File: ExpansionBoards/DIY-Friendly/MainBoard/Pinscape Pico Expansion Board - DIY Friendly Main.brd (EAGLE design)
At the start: 160 x 107 mm, 115 parts, among them IC1 UCC27524P, IC10 ULN2803A, IC11 SN74HC165N, IC12 SN74HC165N, IC13 SN74HC74NE4, IC14 PC827, IC15 S-80833CLY, IC16 SN74HC165N, IC18 SN74HC165N, IC2 UCC27524P, IC3 UCC27524P, IC4 UCC27524P, IC5 UCC27524P, IC6 UCC27524P, IC7 ULN2803A, IC8 ULN2803A, IC9 ULN2803A, J1 30316-6002HBROTATED, J10 215079-4, J11 640454-2, J13 640445-2, J14 SSQ-108-02-T-S-RA, J2 640445-6, J3 640445-5, J4 640445-9, J5 1-640456-0, J6 1-640456-0, J7 1-640456-0, J8 1-640456-0, J9 30308-6002HB, Q1 STP19NF20, Q10 STP19NF20, Q11 STP19NF20, Q12 STP19NF20, Q13 BC337-25, Q15 2N5195G, Q16 2N2222A, Q2 FDPF085N10A, Q3 STP19NF20, Q4 STP19NF20, Q5 STP19NF20, Q6 STP19NF20, Q7 STP19NF20, Q8 STP19NF20, Q9 STP19NF20

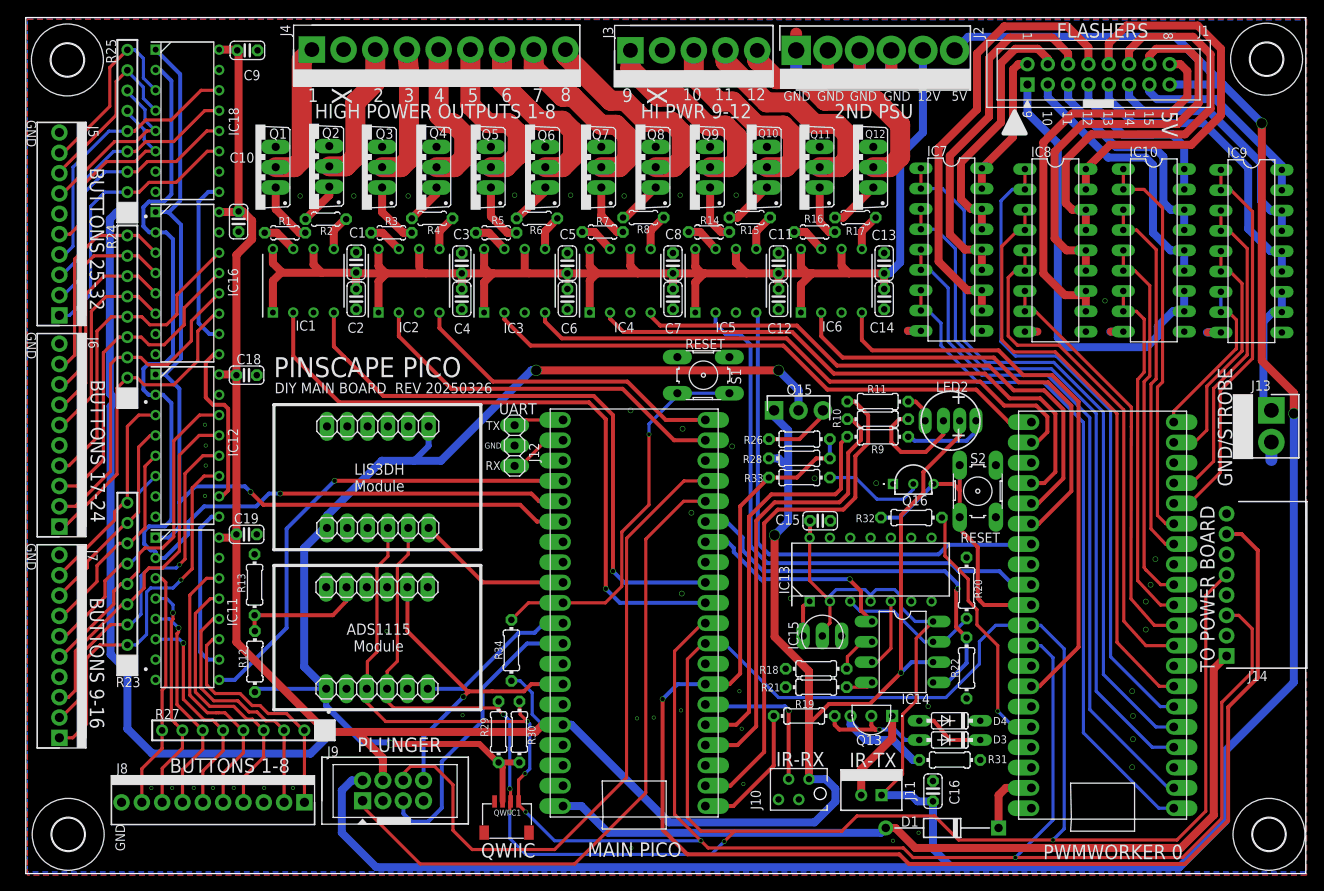
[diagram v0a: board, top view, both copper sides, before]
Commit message: Exp board: DIY main: improve reference designator ordering, fix bypass cap proximities to shift register chips, silkscreen cleanup
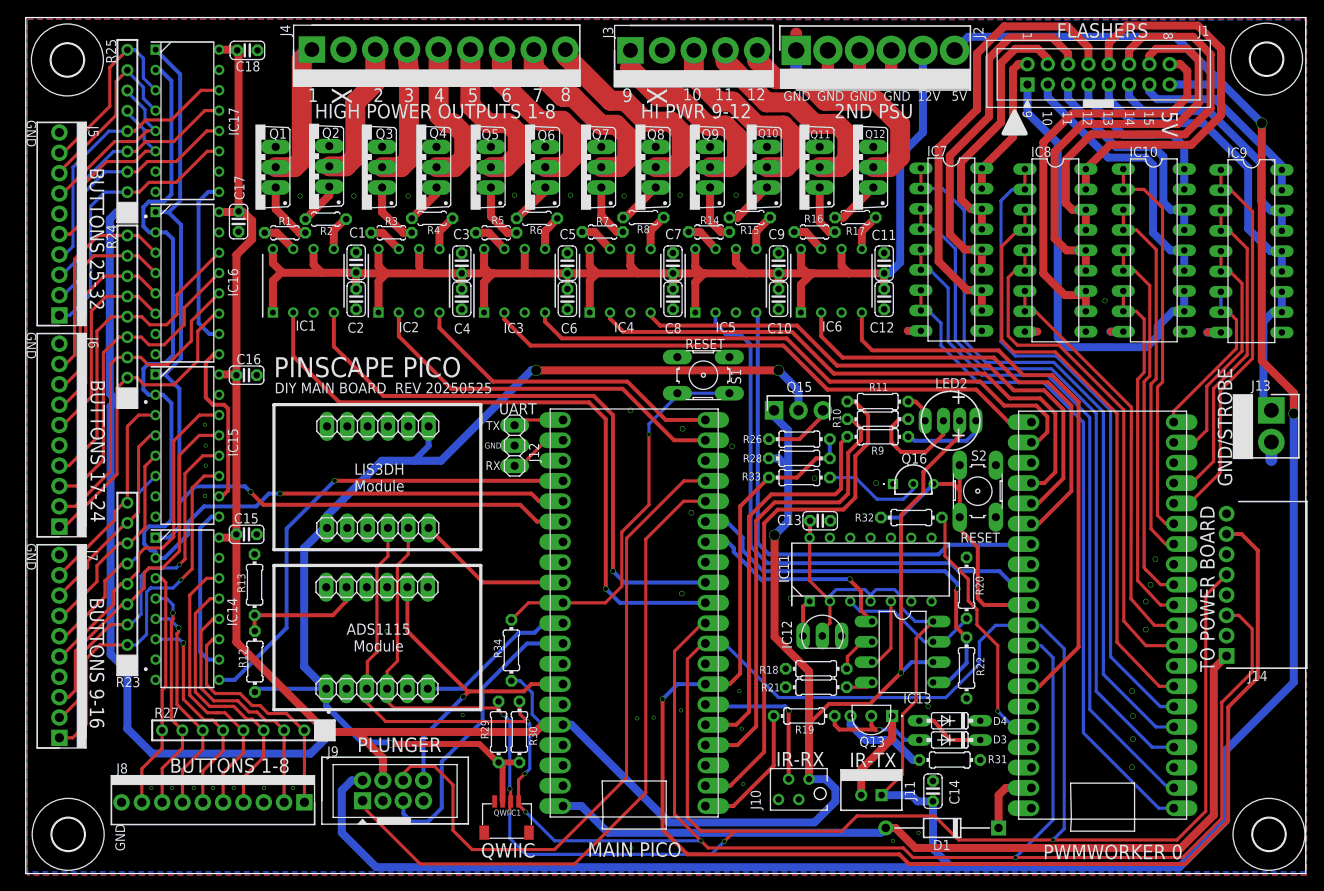
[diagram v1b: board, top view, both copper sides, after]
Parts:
- removed C19: 100nF, rcl:C025-024X044
- added C17: 100nF, rcl:C025-024X044
- C10, C7: value 100nF -> 4.7uF
- C16, C8: value 4.7uF -> 100nF
- IC11: value SN74HC165N -> SN74HC74NE4; device SamacSys_Parts:DIP794W53P254L1930H508Q16N -> SamacSys_Parts:DIP794W53P254L1930H508Q14N
- IC12: value SN74HC165N -> S-80833CLY; device SamacSys_Parts:DIP794W53P254L1930H508Q16N -> SamacSys_Parts:TO-92_(TO-226)
- IC13: value SN74HC74NE4 -> PC827; device SamacSys_Parts:DIP794W53P254L1930H508Q14N -> optocoupler:DIL08
- IC14: value PC827 -> SN74HC165N; device optocoupler:DIL08 -> SamacSys_Parts:DIP794W53P254L1930H508Q16N
- IC15: value S-80833CLY -> SN74HC165N; device SamacSys_Parts:TO-92_(TO-226) -> SamacSys_Parts:DIP794W53P254L1930H508Q16N
- moved C16 100.3 mm to (27.6, 57.3), turned to 180 degrees
- moved IC14 89.6 mm to (20.2, 28.1), turned to 0 degrees
- moved IC11 85.5 mm to (105.6, 33.0), turned to 90 degrees
- moved IC12 81.6 mm to (98.3, 24.7), turned to 180 degrees
- moved IC15 81.6 mm to (20.2, 48.5), turned to 0 degrees
- moved C15 71.7 mm to (27.6, 37.4), turned to 180 degrees
- moved C9 71.5 mm to (94.1, 71.3), turned to 270 degrees
- moved C10 68.2 mm to (94.1, 66.8)
- moved C14 61.8 mm to (113.4, 5.30)
- moved C18 40.6 mm to (27.7, 97.9)
- moved C13 33.2 mm to (99.3, 39.1), turned to 0 degrees
- moved C11 13.2 mm to (107.3, 71.3)
- moved C12 13.2 mm to (107.3, 66.8)
- moved IC13 11.0 mm to (109.6, 22.7), turned to 270 degrees
- moved C7 4.50 mm to (80.9, 71.3), turned to 270 degrees
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- renumbered IC18 to IC17
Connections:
- net 12V: now also C10.2, C9.2; no longer C13.2, C14.2
- net 3V3_PICO: now also C15.2, C16.2, C17.2, IC13.6, IC14.16, IC15.16; no longer C10.2, C19.2, C9.2, IC11.16, IC12.16, IC14.6
- net 5V: now also C13.1, C14.1, IC11.14, IC11.2, IC11.4, IC12.2, IC13.8; no longer C15.1, C16.1, IC13.14, IC13.2, IC13.4, IC14.8, IC15.2
- net BUTTON1: now also IC14.11; no longer IC11.11
- net BUTTON10: now also IC15.12; no longer IC12.12
- net BUTTON11: now also IC15.13; no longer IC12.13
- net BUTTON12: now also IC15.14; no longer IC12.14
- net BUTTON13: now also IC15.6; no longer IC12.6
- net BUTTON14: now also IC15.5; no longer IC12.5
- net BUTTON15: now also IC15.4; no longer IC12.4
- net BUTTON16: now also IC15.3; no longer IC12.3
- net BUTTON2: now also IC14.12; no longer IC11.12
- net BUTTON3: now also IC14.13; no longer IC11.13
- net BUTTON4: now also IC14.14; no longer IC11.14
- net BUTTON5: now also IC14.6; no longer IC11.6
- net BUTTON6: now also IC14.5; no longer IC11.5
- net BUTTON7: now also IC14.4; no longer IC11.4
- net BUTTON8: now also IC14.3; no longer IC11.3
- net BUTTON9: now also IC15.11; no longer IC12.11
- net BUTTON_CLK: now also IC14.2, IC15.2; no longer IC11.2, IC12.2
- net BUTTON_DATA: now also IC14.9; no longer IC11.9
- net BUTTON_SHLD: now also IC14.1, IC15.1; no longer IC11.1, IC12.1
- net GND: now also C13.2, C14.2, C15.1, C16.1, C17.1, IC11.7, IC12.3, IC14.15, IC14.8, IC15.15, IC15.8; no longer C13.1, C14.1, C15.2, C16.2, C19.1, IC11.15, IC11.8, IC12.15, IC12.8, IC13.7, IC15.3
- net N$21: now also IC14.10, IC15.9; no longer IC11.10, IC12.9
- net N$22: now also IC15.10; no longer IC12.10
- net N$58: now also IC11.3, IC13.7; no longer IC13.3, IC14.7
- net N$59: now also IC13.2; no longer IC14.2
- net N$63: now also IC11.1, IC12.1; no longer IC13.1, IC15.1
- net N$65: now also IC13.4; no longer IC14.4
- net N$68: now also IC11.5, IC13.3; no longer IC13.5, IC14.3
- net PSU2_STATUS_SENSE: now also IC13.5; no longer IC14.5
- net PSU2_STATUS_SET: now also IC13.1; no longer IC14.1
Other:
- board text added: "DIY MAIN BOARD REV 20250525"
- board text removed: "DIY MAIN BOARD REV 20250326"

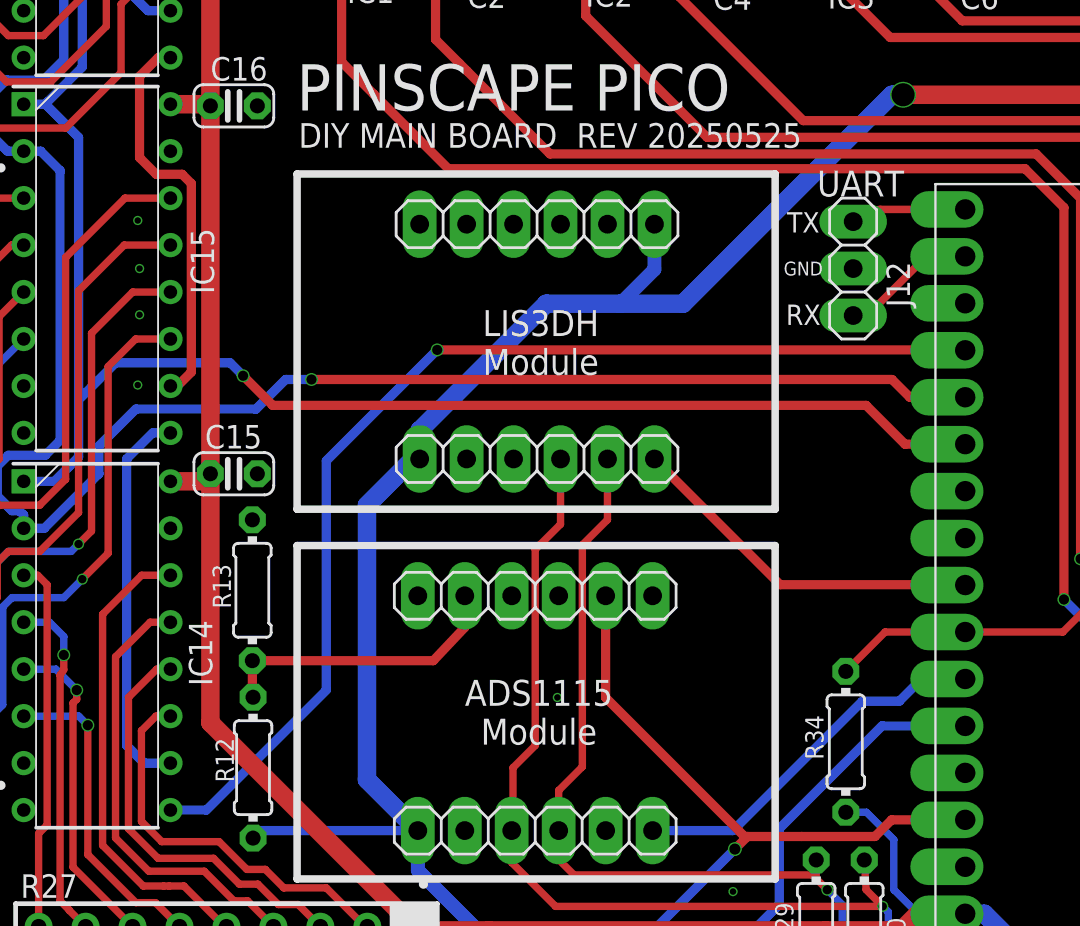
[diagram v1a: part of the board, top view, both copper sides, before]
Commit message: exp board: update BOM for MOSFET recommendations
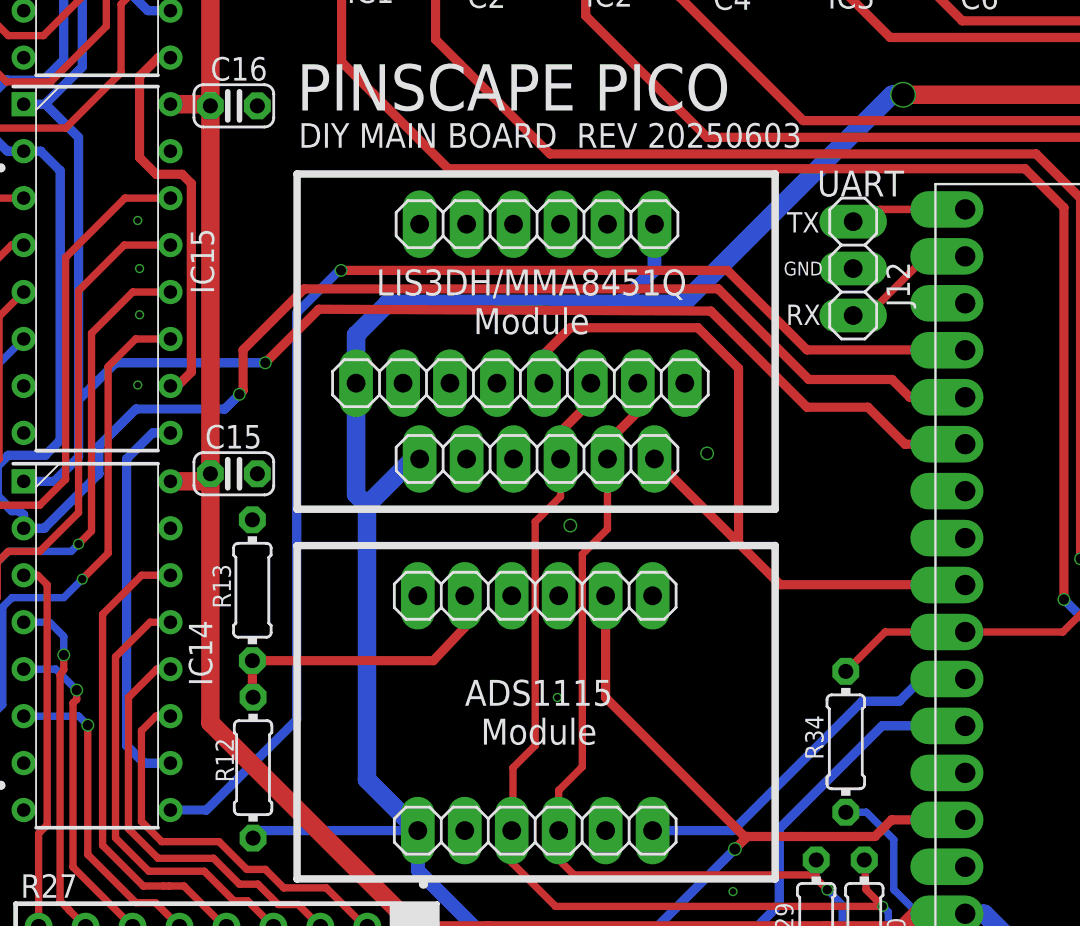
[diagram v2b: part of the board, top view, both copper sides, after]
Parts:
- added JP5: (no value), pinhead:1X08
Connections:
- net 3V3_PERIPHERAL: now also JP5.1
- net ACCEL_INTR: now also JP5.5
- net GND: now also JP5.2
- net SCL: now also JP5.6
- net SDA: now also JP5.7
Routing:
- net ACCEL_INTR: track 19.6 -> 42.7 mm
- net 3V3_PERIPHERAL: track 142.6 -> 151.8 mm
- net BUTTON_DATA: track 60.6 -> 69.8 mm
- net BUTTON_CLK: track 131.7 -> 137.0 mm
- net SDA: track 287.6 -> 292.4 mm
- net SCL: track 240.4 -> 245.2 mm
- net BUTTON_SHLD: track 120.8 -> 123.2 mm
- net GND: vias 48 -> 50
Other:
- board text added: "DIY MAIN BOARD REV 20250603"
- board text added: "LIS3DH/MMA8451Q Module"
- board text removed: "DIY MAIN BOARD REV 20250525"
- board text removed: "LIS3DH Module"

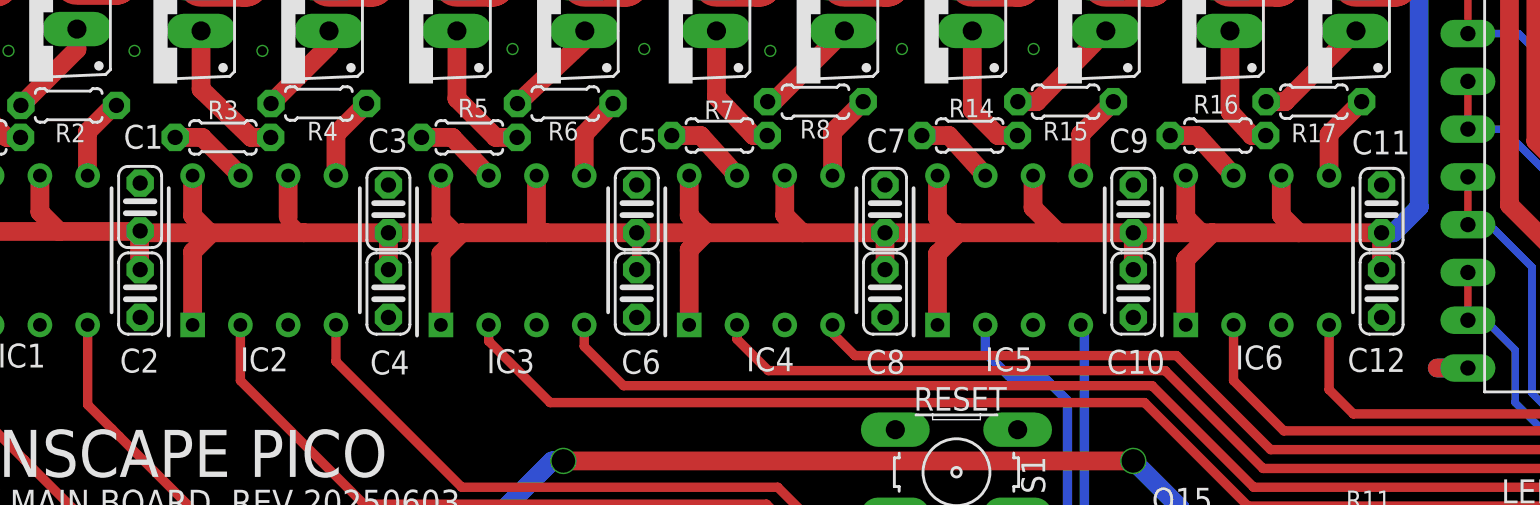
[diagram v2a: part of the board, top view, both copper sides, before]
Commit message: exp board: DIY main: fix C7/C8 reversal
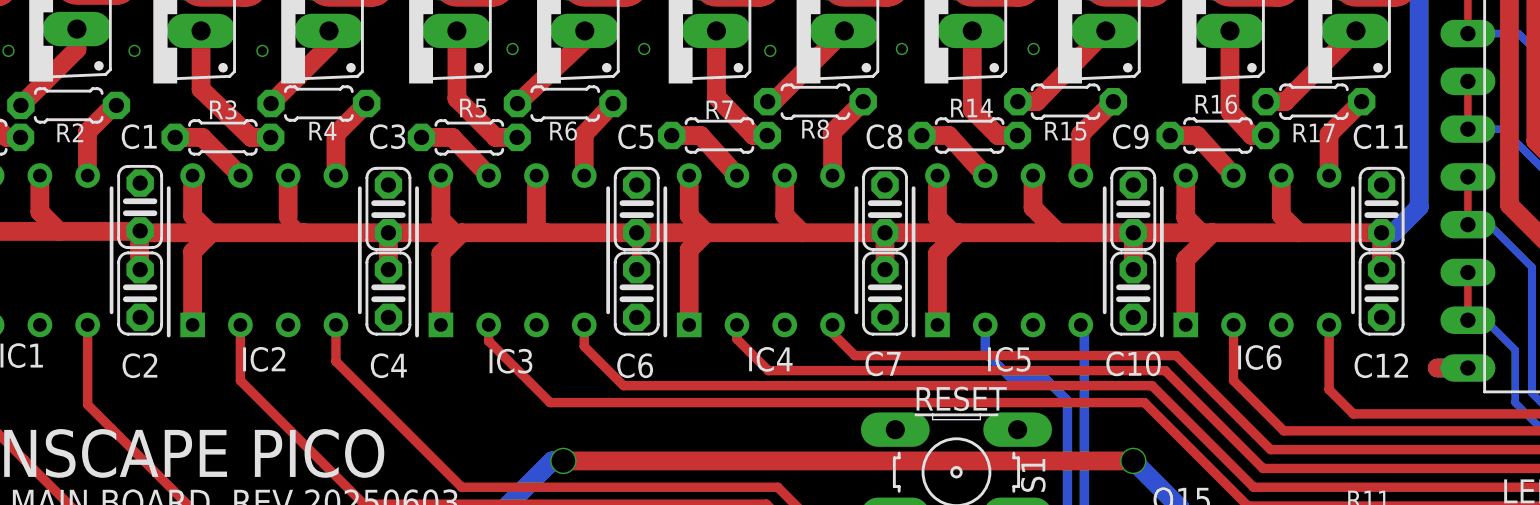
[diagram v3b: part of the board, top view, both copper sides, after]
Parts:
- moved C7 4.50 mm to (80.9, 66.8), turned to 90 degrees
- moved C8 4.50 mm to (80.9, 71.3), turned to 270 degrees
